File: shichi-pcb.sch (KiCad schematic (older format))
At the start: 27 parts, among them J1 USB_C_Receptacle_HRO_TYPE-C-3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, J2 Conn_01x04_Male, J3 Conn_01x06_Male, J4 Conn_01x04_Male, J5 Conn_01x02_Male, J6 Conn_01x01_Male, SW1 SW_Push, SW2 SW_Push, U1 MCP1700-3302E_SOT23, U2 USBLC6-2SC6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

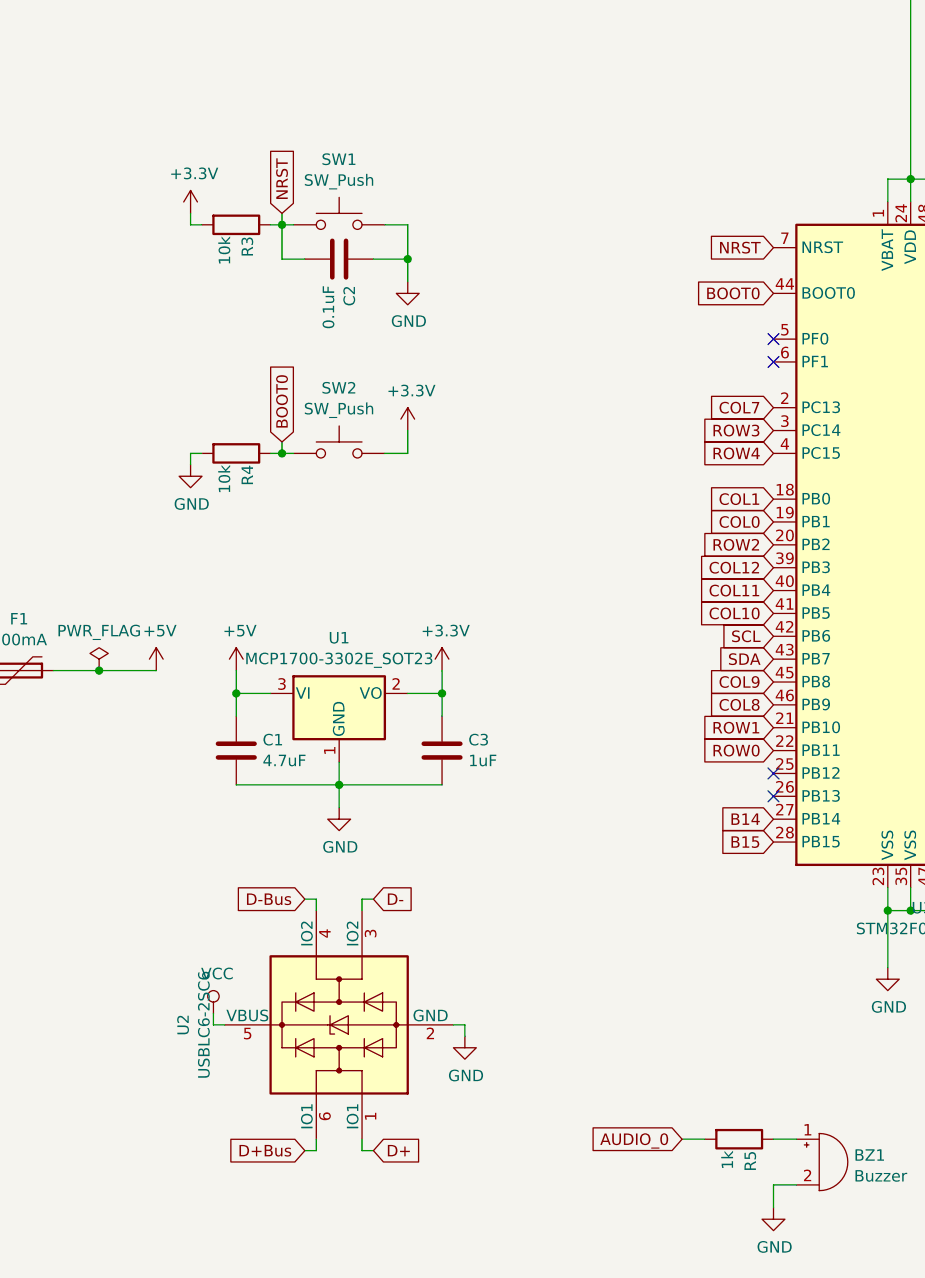
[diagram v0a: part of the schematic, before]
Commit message: Remove NRST pull-up resistor
The NRST pin input driver uses the CMOS technology. It is connected to a permanent pullup resistor, RPU
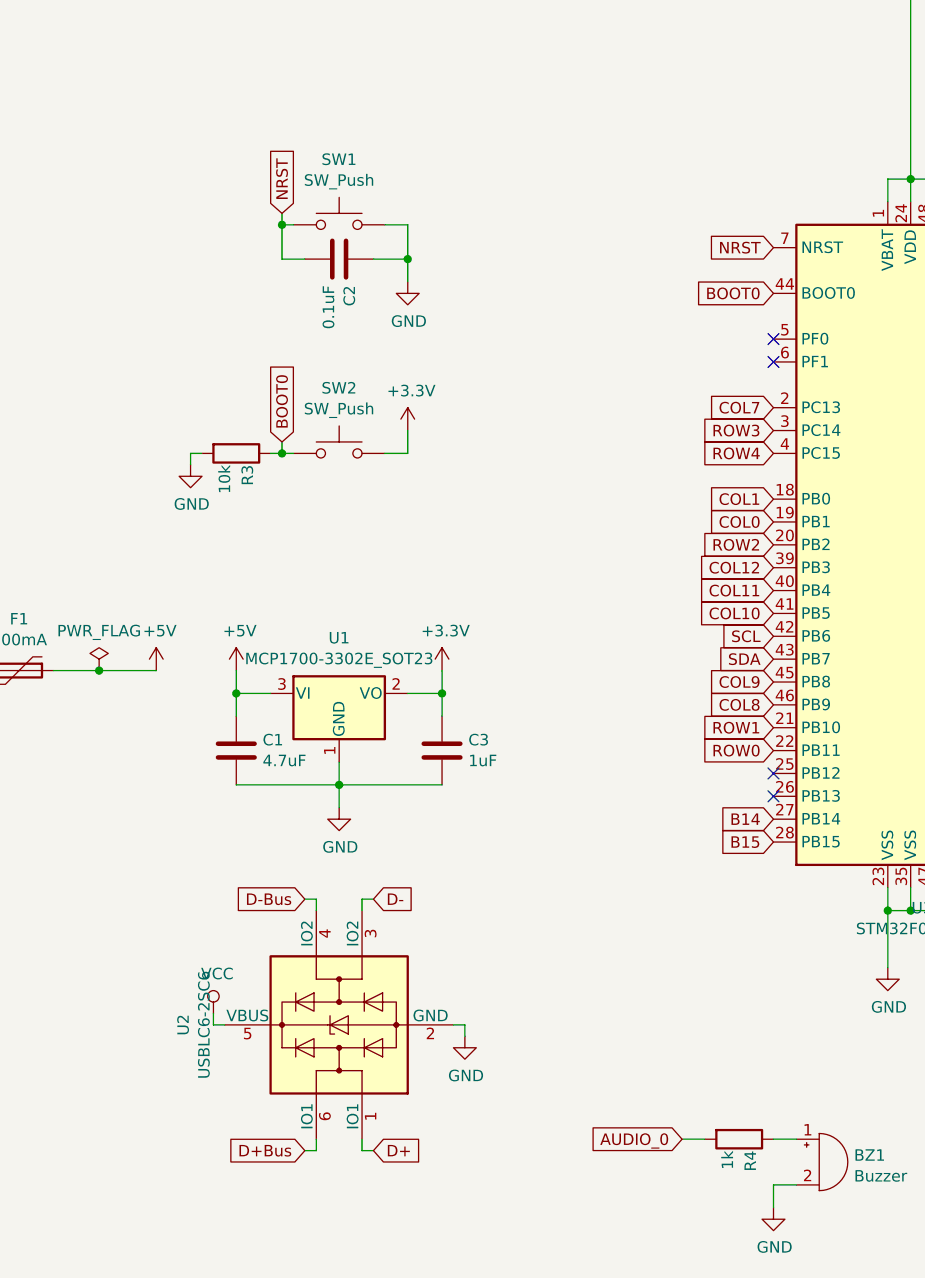
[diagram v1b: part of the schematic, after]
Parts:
- removed R3: 10k, Resistor_SMD:R_0805_2012Metric_Pad1.15x1.40mm_HandSolder, symbol Device:R
- renumbered R4 to R3, R5 to R4
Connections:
- wire segments 88 -> 85
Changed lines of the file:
@@
-$EndComp
-$Comp
-L Switch:SW_Push SW1
-U 1 1 5CFF60B9
-P 4000 3000
-F 0 "SW1" H 4000 3285 50  0000 C CNN
-F 1 "SW_Push" H 4000 3194 50  0000 C CNN
-F 2 "Button_Switch_SMD:SW_SPST_TL3342" H 4000 3200 50  0001 C CNN
-F 3 "~" H 4000 3200 50  0001 C CNN
-	1    4000 3000
-	1    0    0    -1
 $EndComp
 $Comp
@@
 $EndComp
 $Comp
-L power:GND #PWR012
+L power:GND #PWR011
 U 1 1 5CFB408D
 P 4300 3250
-F 0 "#PWR012" H 4300 3000 50  0001 C CNN
+F 0 "#PWR011" H 4300 3000 50  0001 C CNN
 F 1 "GND" H 4305 3077 50  0000 C CNN
 F 2 "" H 4300 3250 50  0001 C CNN
@@
 $EndComp
 $Comp
-L power:GND #PWR021
+L power:GND #PWR020
 U 1 1 5CFB6455
 P 7300 1700
-F 0 "#PWR021" H 7300 1450 50  0001 C CNN
+F 0 "#PWR020" H 7300 1450 50  0001 C CNN
 F 1 "GND" H 7305 1527 50  0000 C CNN
 F 2 "" H 7300 1700 50  0001 C CNN
@@
 SDA
 $Comp
-L power:GND #PWR030
+L power:GND #PWR029
 U 1 1 5D01D767
 P 10500 2400
-F 0 "#PWR030" H 10500 2150 50  0001 C CNN
+F 0 "#PWR029" H 10500 2150 50  0001 C CNN
 F 1 "GND" H 10505 2227 50  0000 C CNN
 F 2 "" H 10500 2400 50  0001 C CNN
@@
 	4500 6500 4550 6500
 $Comp
-L power:GND #PWR015
+L power:GND #PWR014
 U 1 1 5D32B978
 P 4550 6550
-F 0 "#PWR015" H 4550 6300 50  0001 C CNN
+F 0 "#PWR014" H 4550 6300 50  0001 C CNN
 F 1 "GND" H 4555 6377 50  0000 C CNN
 F 2 "" H 4550 6550 50  0001 C CNN
@@
 	3450 6500 3500 6500
 $Comp
-L power:VCC #PWR09
+L power:VCC #PWR08
 U 1 1 5D31D96D
 P 3450 6450
-F 0 "#PWR09" H 3450 6300 50  0001 C CNN
+F 0 "#PWR08" H 3450 6300 50  0001 C CNN
 F 1 "VCC" H 3467 6623 50  0000 C CNN
 F 2 "" H 3450 6450 50  0001 C CNN
@@
 	4450 5050 4450 5150
 $Comp
-L power:+3.3V #PWR014
+L power:+3.3V #PWR013
 U 1 1 5D1ECA69
 P 4450 4950
-F 0 "#PWR014" H 4450 4800 50  0001 C CNN
+F 0 "#PWR013" H 4450 4800 50  0001 C CNN
 F 1 "+3.3V" H 4465 5123 50  0000 C CNN
 F 2 "" H 4450 4950 50  0001 C CNN
@@
 Connection ~ 4450 5050
 $Comp
-L power:GND #PWR011
+L power:GND #PWR010
 U 1 1 5D1FE5B6
 P 4000 5550
-F 0 "#PWR011" H 4000 5300 50  0001 C CNN
+F 0 "#PWR010" H 4000 5300 50  0001 C CNN
 F 1 "GND" H 4005 5377 50  0000 C CNN
 F 2 "" H 4000 5550 50  0001 C CNN
@@
 Wire Wire Line
 	4000 5450 4000 5550
-$Comp
-L power:+3.3V #PWR07
-U 1 1 5D234A14
-P 3350 2950
-F 0 "#PWR07" H 3350 2800 50  0001 C CNN
-F 1 "+3.3V" H 3365 3123 50  0000 C CNN
-F 2 "" H 3350 2950 50  0001 C CNN
-F 3 "" H 3350 2950 50  0001 C CNN
-	1    3350 2950
-	1    0    0    -1
-$EndComp
 Wire Wire Line
 	4200 3000 4300 3000
 Wire Wire Line
 	4300 3000 4300 3150
-Wire Wire Line
-	3350 2950 3350 3000
-Wire Wire Line
-	3350 3000 3400 3000
-$Comp
-L Device:R R3
-U 1 1 5CFF36BA
-P 3550 3000
-F 0 "R3" H 3600 3050 50  0000 L CNN
-F 1 "10k" H 3600 2950 50  0000 L CNN
-F 2 "Resistor_SMD:R_0805_2012Metric_Pad1.15x1.40mm_HandSolder" V 3480 3000 50  0001 C CNN
-F 3 "~" H 3550 3000 50  0001 C CNN
-	1    3550 3000
-	0    1    1    0
-$EndComp
-Wire Wire Line
-	3700 3000 3750 3000
 $Comp
 L Device:C C2
@@
 Wire Wire Line
 	3850 3150 3750 3150
-Wire Wire Line
-	3750 3150 3750 3000
-Connection ~ 3750 3000
-Wire Wire Line
-	3750 3000 3800 3000
 Text GLabel 3750 2950 1    50   Input ~ 0
 NRST
-Wire Wire Line
-	3750 2950 3750 3000
 $Comp
 L Switch:SW_Push SW2
@@
 $EndComp
 $Comp
-L power:GND #PWR08
+L power:GND #PWR07
 U 1 1 5D281CF4
 P 3350 4050
-F 0 "#PWR08" H 3350 3800 50  0001 C CNN
+F 0 "#PWR07" H 3350 3800 50  0001 C CNN
 F 1 "GND" H 3355 3877 50  0000 C CNN
 F 2 "" H 3350 4050 50  0001 C CNN
@@
 $EndComp
 $Comp
-L power:+3.3V #PWR013
+L power:+3.3V #PWR012
 U 1 1 5D281CFA
 P 4300 3900
-F 0 "#PWR013" H 4300 3750 50  0001 C CNN
+F 0 "#PWR012" H 4300 3750 50  0001 C CNN
 F 1 "+3.3V" H 4315 4073 50  0000 C CNN
 F 2 "" H 4300 3900 50  0001 C CNN
@@
 	3350 4000 3400 4000
 $Comp
-L Device:R R4
+L Device:R R3
 U 1 1 5D281D04
 P 3550 4000
-F 0 "R4" H 3600 4050 50  0000 L CNN
+F 0 "R3" H 3600 4050 50  0000 L CNN
 F 1 "10k" H 3600 3950 50  0000 L CNN
 F 2 "Resistor_SMD:R_0805_2012Metric_Pad1.15x1.40mm_HandSolder" V 3480 4000 50  0001 C CNN
@@
 	6700 1950 7300 1950
 $Comp
-L power:GND #PWR022
+L power:GND #PWR021
 U 1 1 5CFB5A7D
 P 7300 2250
-F 0 "#PWR022" H 7300 2000 50  0001 C CNN
+F 0 "#PWR021" H 7300 2000 50  0001 C CNN
 F 1 "GND" H 7305 2077 50  0000 C CNN
 F 2 "" H 7300 2250 50  0001 C CNN
@@
 $EndComp
 $Comp
-L power:GND #PWR025
+L power:GND #PWR024
 U 1 1 5CFB56F6
 P 7700 2800
-F 0 "#PWR025" H 7700 2550 50  0001 C CNN
+F 0 "#PWR024" H 7700 2550 50  0001 C CNN
 F 1 "GND" H 7705 2627 50  0000 C CNN
 F 2 "" H 7700 2800 50  0001 C CNN
@@
 $EndComp
 $Comp
-L power:GND #PWR023
+L power:GND #PWR022
 U 1 1 5CFB4E50
 P 7300 2800
-F 0 "#PWR023" H 7300 2550 50  0001 C CNN
+F 0 "#PWR022" H 7300 2550 50  0001 C CNN
 F 1 "GND" H 7305 2627 50  0000 C CNN
 F 2 "" H 7300 2800 50  0001 C CNN
@@
 Connection ~ 7300 1400
 $Comp
-L power:GND #PWR024
+L power:GND #PWR023
 U 1 1 5D2D41CB
 P 7700 1700
-F 0 "#PWR024" H 7700 1450 50  0001 C CNN
+F 0 "#PWR023" H 7700 1450 50  0001 C CNN
 F 1 "GND" H 7705 1527 50  0000 C CNN
 F 2 "" H 7700 1700 50  0001 C CNN
@@
 Connection ~ 7700 1400
 $Comp
-L power:GND #PWR026
+L power:GND #PWR025
 U 1 1 5D2DADBD
 P 8100 1700
-F 0 "#PWR026" H 8100 1450 50  0001 C CNN
+F 0 "#PWR025" H 8100 1450 50  0001 C CNN
 F 1 "GND" H 8105 1527 50  0000 C CNN
 F 2 "" H 8100 1700 50  0001 C CNN
@@
 $EndComp
 $Comp
-L power:+3.3V #PWR018
+L power:+3.3V #PWR017
 U 1 1 5D2DDDA7
 P 6500 1400
-F 0 "#PWR018" H 6500 1250 50  0001 C CNN
+F 0 "#PWR017" H 6500 1250 50  0001 C CNN
 F 1 "+3.3V" H 6515 1573 50  0000 C CNN
 F 2 "" H 6500 1400 50  0001 C CNN
@@
 Connection ~ 6500 1400
 $Comp
-L power:+3.3V #PWR019
+L power:+3.3V #PWR018
 U 1 1 5D2DEB65
 P 6700 1950
-F 0 "#PWR019" H 6700 1800 50  0001 C CNN
+F 0 "#PWR018" H 6700 1800 50  0001 C CNN
 F 1 "+3.3V" H 6715 2123 50  0000 C CNN
 F 2 "" H 6700 1950 50  0001 C CNN
@@
 Connection ~ 6700 1950
 $Comp
-L power:+3.3V #PWR020
+L power:+3.3V #PWR019
 U 1 1 5D2DF334
 P 6800 2500
-F 0 "#PWR020" H 6800 2350 50  0001 C CNN
+F 0 "#PWR019" H 6800 2350 50  0001 C CNN
 F 1 "+3.3V" H 6815 2673 50  0000 C CNN
 F 2 "" H 6800 2500 50  0001 C CNN
@@
 SCL
 $Comp
-L power:+3.3V #PWR028
+L power:+3.3V #PWR026
 U 1 1 5D2F0717
 P 10500 1100
-F 0 "#PWR028" H 10500 950 50  0001 C CNN
+F 0 "#PWR026" H 10500 950 50  0001 C CNN
 F 1 "+3.3V" V 10515 1228 50  0000 L CNN
 F 2 "" H 10500 1100 50  0001 C CNN
@@
 SWCLK
 $Comp
-L power:+5V #PWR029
+L power:+5V #PWR028
 U 1 1 5D305D9D
 P 10500 2300
-F 0 "#PWR029" H 10500 2150 50  0001 C CNN
+F 0 "#PWR028" H 10500 2150 50  0001 C CNN
 F 1 "+5V" V 10515 2428 50  0000 L CNN
 F 2 "" H 10500 2300 50  0001 C CNN
@@
 $EndComp
 $Comp
-L power:+5V #PWR010
+L power:+5V #PWR09
 U 1 1 5D30778B
 P 3550 4950
-F 0 "#PWR010" H 3550 4800 50  0001 C CNN
+F 0 "#PWR09" H 3550 4800 50  0001 C CNN
 F 1 "+5V" H 3565 5123 50  0000 C CNN
 F 2 "" H 3550 4950 50  0001 C CNN
@@
 B15
 $Comp
-L power:GND #PWR017
+L power:GND #PWR016
 U 1 1 5D30B602
 P 6400 6250
-F 0 "#PWR017" H 6400 6000 50  0001 C CNN
+F 0 "#PWR016" H 6400 6000 50  0001 C CNN
 F 1 "GND" H 6405 6077 50  0000 C CNN
 F 2 "" H 6400 6250 50  0001 C CNN
@@
 AUDIO_0
 $Comp
-L Device:R R5
+L Device:R R4
 U 1 1 5D35C35E
 P 5750 7000
-F 0 "R5" H 5800 7050 50  0000 L CNN
+F 0 "R4" H 5800 7050 50  0000 L CNN
 F 1 "1k" H 5800 6950 50  0000 L CNN
 F 2 "Resistor_SMD:R_0805_2012Metric_Pad1.15x1.40mm_HandSolder" V 5680 7000 50  0001 C CNN
@@
 	5600 7000 5500 7000
 $Comp
-L power:GND #PWR016
+L power:GND #PWR015
 U 1 1 5D361771
 P 5900 7300
-F 0 "#PWR016" H 5900 7050 50  0001 C CNN
+F 0 "#PWR015" H 5900 7050 50  0001 C CNN
 F 1 "GND" H 5905 7127 50  0000 C CNN
 F 2 "" H 5900 7300 50  0001 C CNN
@@
 	1    0    0    -1
 $EndComp
+$Comp
+L Switch:SW_Push SW1
+U 1 1 5CFF60B9
+P 4000 3000
+F 0 "SW1" H 4000 3285 50  0000 C CNN
+F 1 "SW_Push" H 4000 3194 50  0000 C CNN
+F 2 "Button_Switch_SMD:SW_SPST_TL3342" H 4000 3200 50  0001 C CNN
+F 3 "~" H 4000 3200 50  0001 C CNN
+	1    4000 3000
+	1    0    0    -1
+$EndComp
+Wire Wire Line
+	3750 2950 3750 3000
+Wire Wire Line
+	3750 3150 3750 3000
+Connection ~ 3750 3000
+Wire Wire Line
+	3750 3000 3800 3000
 $EndSCHEMATC

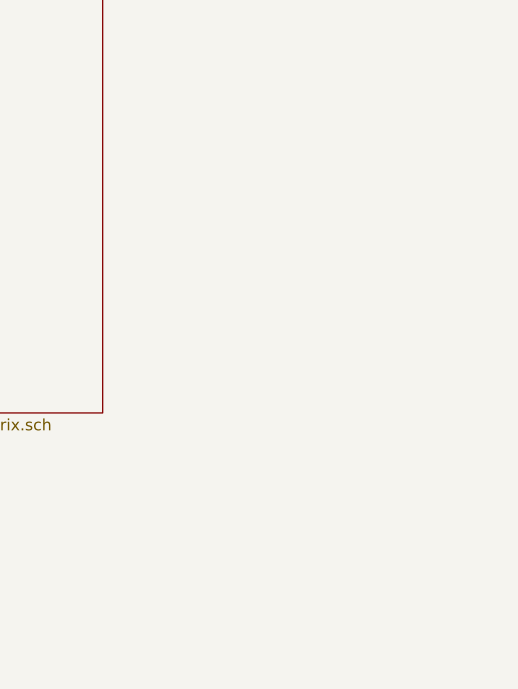
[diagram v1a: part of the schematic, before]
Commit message: Add mounting holes
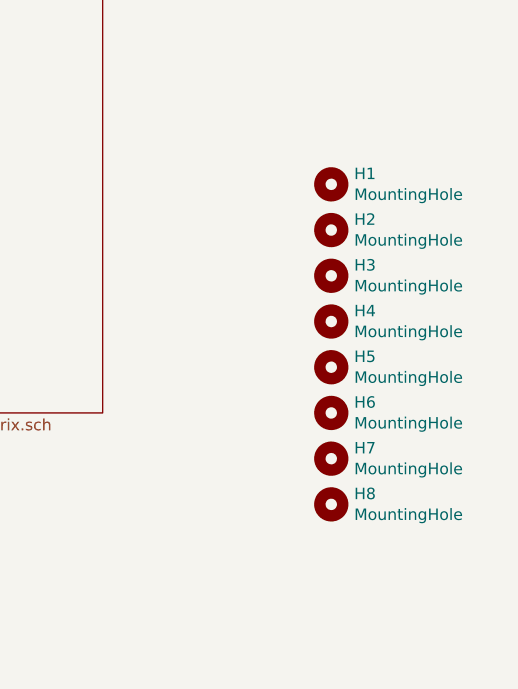
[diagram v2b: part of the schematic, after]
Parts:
- added H1, H2, H3, H4, H5, H6, H7, H8: MountingHole, MountingHole:MountingHole_2.2mm_M2_Pad, symbol Mechanical:MountingHole
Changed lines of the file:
@@
 Wire Wire Line
 	3750 3000 3800 3000
+$Comp
+L Mechanical:MountingHole H1
+U 1 1 5D286FF1
+P 10250 4500
+F 0 "H1" H 10350 4546 50  0000 L CNN
+F 1 "MountingHole" H 10350 4455 50  0000 L CNN
+F 2 "MountingHole:MountingHole_2.2mm_M2_Pad" H 10250 4500 50  0001 C CNN
+F 3 "~" H 10250 4500 50  0001 C CNN
+	1    10250 4500
+	1    0    0    -1
+$EndComp
+$Comp
+L Mechanical:MountingHole H2
+U 1 1 5D289B87
+P 10250 4700
+F 0 "H2" H 10350 4746 50  0000 L CNN
+F 1 "MountingHole" H 10350 4655 50  0000 L CNN
+F 2 "MountingHole:MountingHole_2.2mm_M2_Pad" H 10250 4700 50  0001 C CNN
+F 3 "~" H 10250 4700 50  0001 C CNN
+	1    10250 4700
+	1    0    0    -1
+$EndComp
+$Comp
+L Mechanical:MountingHole H3
+U 1 1 5D28A2AE
+P 10250 4900
+F 0 "H3" H 10350 4946 50  0000 L CNN
+F 1 "MountingHole" H 10350 4855 50  0000 L CNN
+F 2 "MountingHole:MountingHole_2.2mm_M2_Pad" H 10250 4900 50  0001 C CNN
+F 3 "~" H 10250 4900 50  0001 C CNN
+	1    10250 4900
+	1    0    0    -1
+$EndComp
+$Comp
+L Mechanical:MountingHole H4
+U 1 1 5D28A525
+P 10250 5100
+F 0 "H4" H 10350 5146 50  0000 L CNN
+F 1 "MountingHole" H 10350 5055 50  0000 L CNN
+F 2 "MountingHole:MountingHole_2.2mm_M2_Pad" H 10250 5100 50  0001 C CNN
+F 3 "~" H 10250 5100 50  0001 C CNN
+	1    10250 5100
+	1    0    0    -1
+$EndComp
+$Comp
+L Mechanical:MountingHole H5
+U 1 1 5D28A77B
+P 10250 5300
+F 0 "H5" H 10350 5346 50  0000 L CNN
+F 1 "MountingHole" H 10350 5255 50  0000 L CNN
+F 2 "MountingHole:MountingHole_2.2mm_M2_Pad" H 10250 5300 50  0001 C CNN
+F 3 "~" H 10250 5300 50  0001 C CNN
+	1    10250 5300
+	1    0    0    -1
+$EndComp
+$Comp
+L Mechanical:MountingHole H6
+U 1 1 5D28A98E
+P 10250 5500
+F 0 "H6" H 10350 5546 50  0000 L CNN
+F 1 "MountingHole" H 10350 5455 50  0000 L CNN
+F 2 "MountingHole:MountingHole_2.2mm_M2_Pad" H 10250 5500 50  0001 C CNN
+F 3 "~" H 10250 5500 50  0001 C CNN
+	1    10250 5500
+	1    0    0    -1
+$EndComp
+$Comp
+L Mechanical:MountingHole H7
+U 1 1 5D28ABAE
+P 10250 5700
+F 0 "H7" H 10350 5746 50  0000 L CNN
+F 1 "MountingHole" H 10350 5655 50  0000 L CNN
+F 2 "MountingHole:MountingHole_2.2mm_M2_Pad" H 10250 5700 50  0001 C CNN
+F 3 "~" H 10250 5700 50  0001 C CNN
+	1    10250 5700
+	1    0    0    -1
+$EndComp
+$Comp
+L Mechanical:MountingHole H8
+U 1 1 5D28AE2C
+P 10250 5900
+F 0 "H8" H 10350 5946 50  0000 L CNN
+F 1 "MountingHole" H 10350 5855 50  0000 L CNN
+F 2 "MountingHole:MountingHole_2.2mm_M2_Pad" H 10250 5900 50  0001 C CNN
+F 3 "~" H 10250 5900 50  0001 C CNN
+	1    10250 5900
+	1    0    0    -1
+$EndComp
 $EndSCHEMATC
